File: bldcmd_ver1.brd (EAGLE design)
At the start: 43 x 49 mm, 90 parts, among them CN1 DF61-2P-2.2V(23), CN2 DF65-3P-1.7V(21), CN3 SM05B-SRSS-TB, CN4 SM04B-SRSS-TB, CN6 SM05B-SRSS-TB, CN7 SM04B-SRSS-TB, IC1 STSPIN32F0A, IC2 AS5047P-ATSM, IC3 ADM4852ACPZ-REEL7, Q1 PSMN2R4-30MLD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

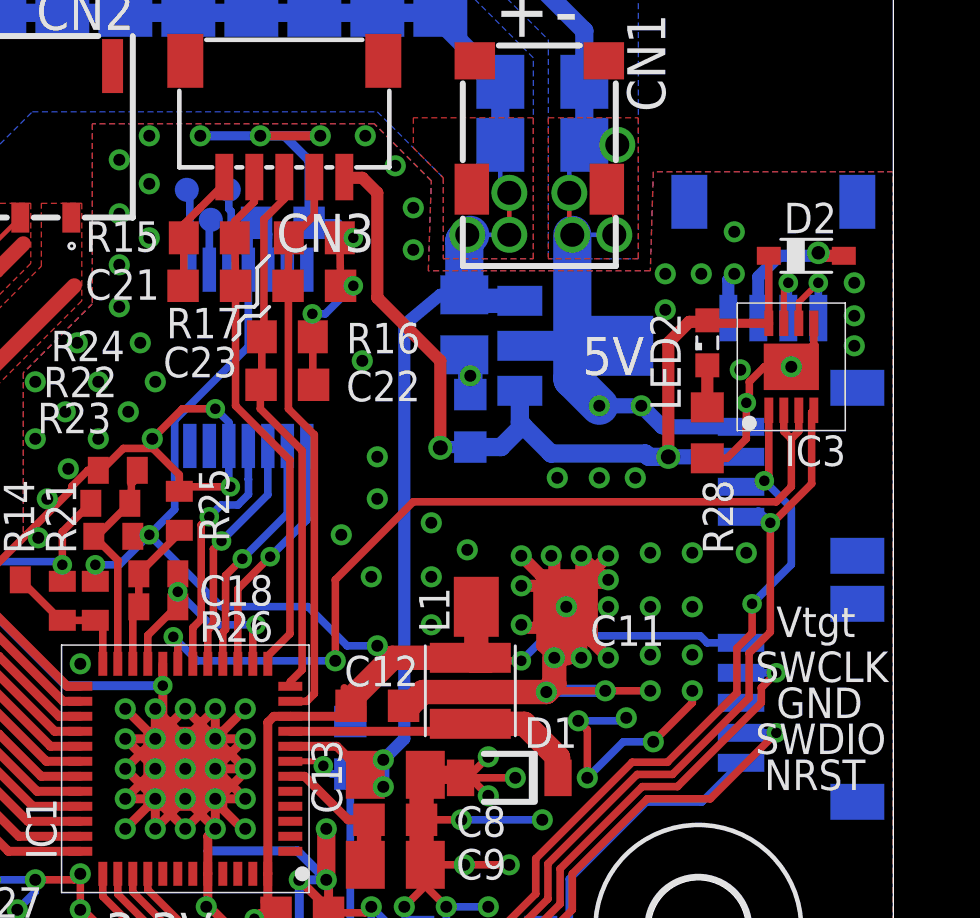
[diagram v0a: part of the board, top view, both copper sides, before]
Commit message: 部品に必要な値を割り当てた，（最適なのか？） BOM出した
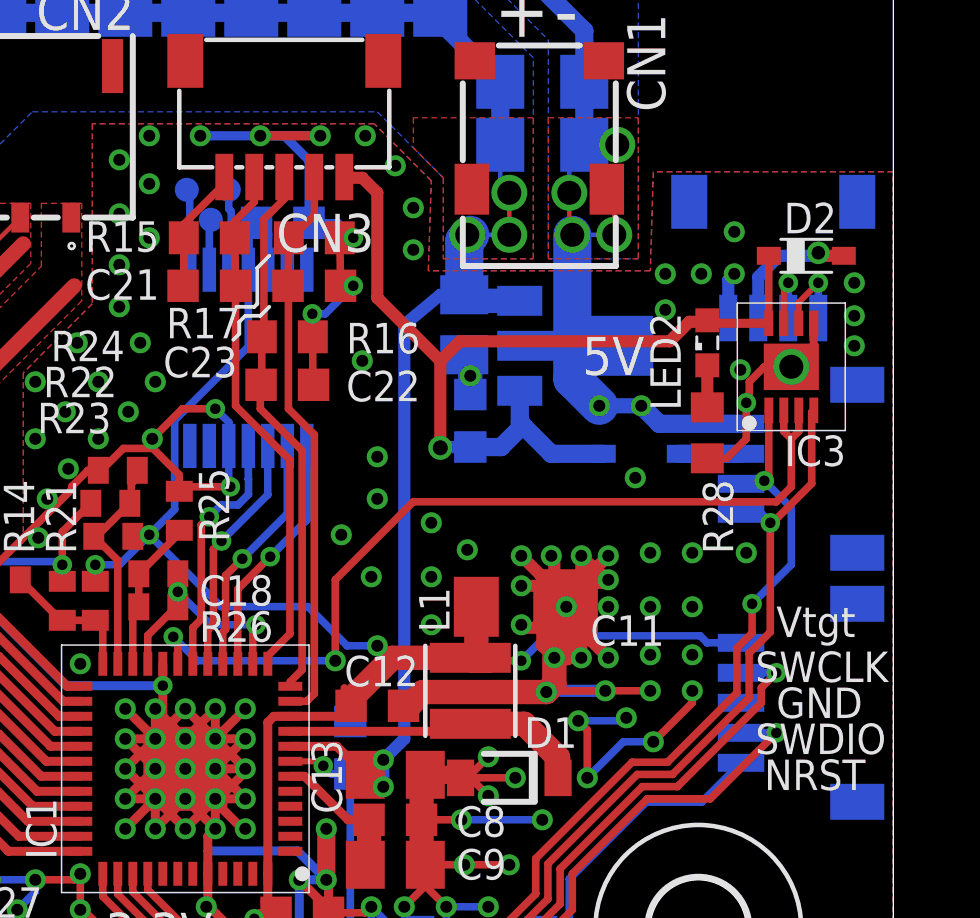
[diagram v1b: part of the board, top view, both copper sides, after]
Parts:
- removed CN4: SM04B-SRSS-TB, scramble-con-jst:SM04B-SRSS-TB
- added CN5: SM04B-SRSS-TB, scramble-con-jst:SM04B-SRSS-TB
- added D3: BAT60J, diode:SOD323_ST
- C1, C2, C3: value (none) -> 0.1u
- C17, C18: value (none) -> 100p
- L1: device rcssl_lib:SRN3015 -> scramble-mcu:SRN3015
- R1, R2, R3, R4, R5, R6: value (none) -> 20
- R10, R11, R12, R29, R7, R8, R9: value (none) -> 10k
- R14, R26: value (none) -> 15k
- R21: value (none) -> NP
- R22, R24: value (none) -> 560
- R23: value (none) -> 8.2k
- R25, R27, R28: value (none) -> 1k
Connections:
- new net N$10: CN5.2, D3.A
- net +5V: now also D3.C; no longer CN4.2
- net GND: now also CN5.1; no longer CN4.1
- net UART_RX: now also CN5.3; no longer CN4.3
- net UART_TX: now also CN5.4; no longer CN4.4
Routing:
- net N$10: track 0.00 -> 2.07 mm
- net +5V: track 32.4 -> 31.8 mm, vias 2 -> 1
- net GND: vias 149 -> 147

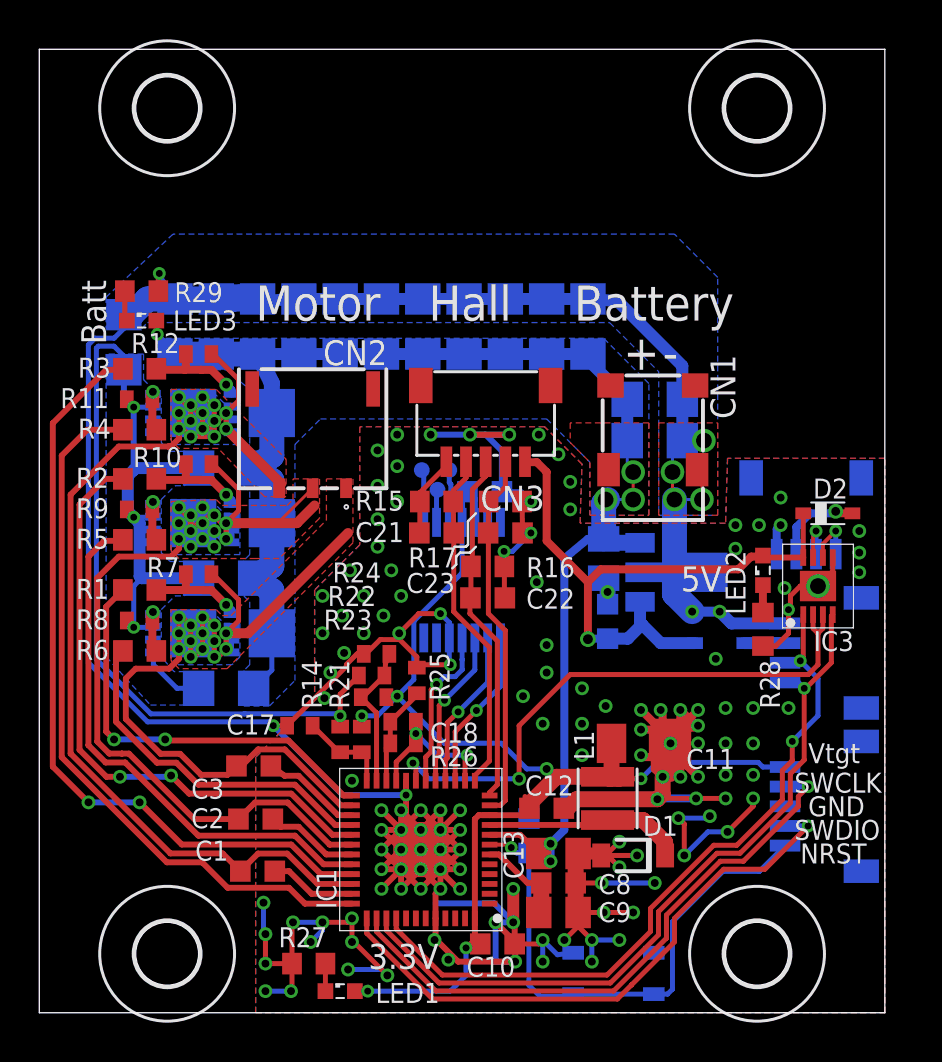
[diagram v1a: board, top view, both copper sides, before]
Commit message: AWを修正，コネクタの変更を適用
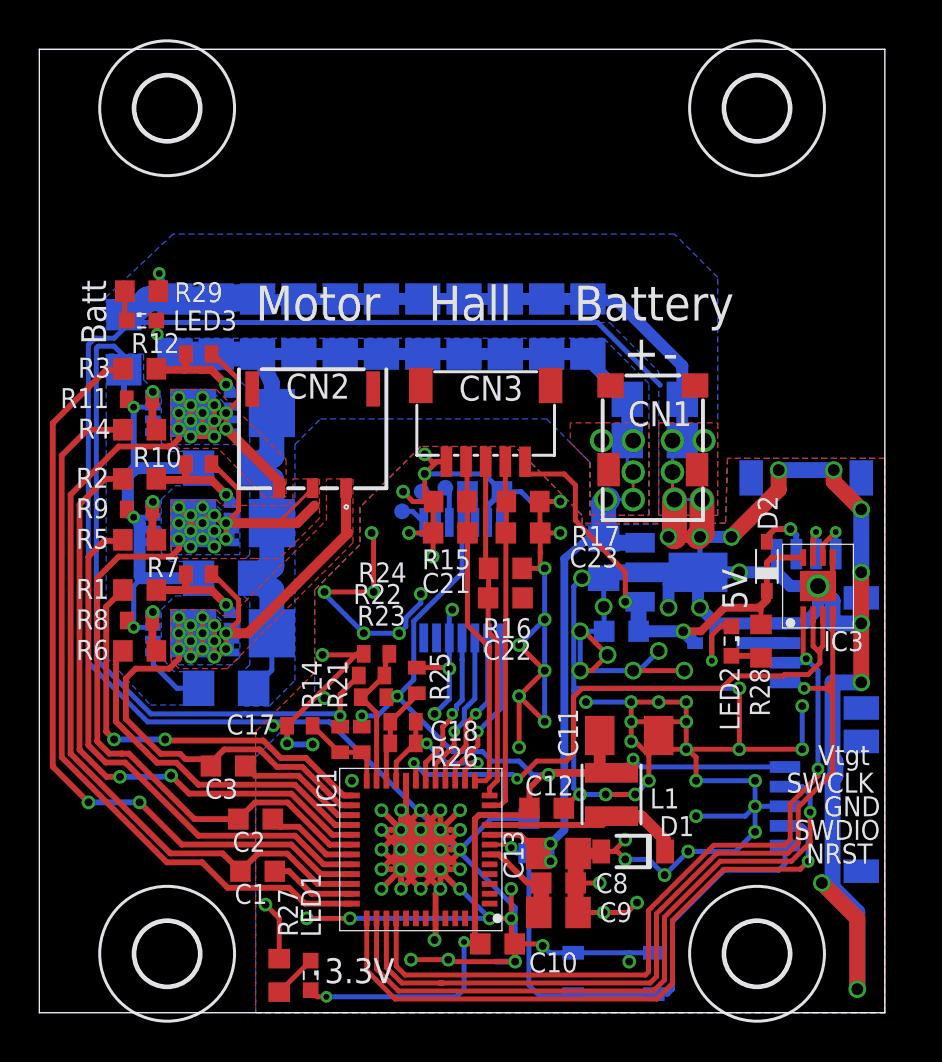
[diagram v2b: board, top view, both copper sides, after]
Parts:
- moved D2 4.11 mm to (37.0, 22.7), turned to 90 degrees
- moved LED2 3.94 mm to (35.2, 18.9), turned to 270 degrees
- moved TP3 2.33 mm to (18.4, 25.5)
- moved LED1 1.70 mm to (13.8, 1.90), turned to 270 degrees
- moved R27 1.62 mm to (12.2, 1.90), turned to 270 degrees
- moved C3 1.30 mm to (9.60, 12.6)
- moved TP1 0.92 mm to (20.6, 26.7)
- moved R16 0.91 mm to (23.7, 22.6)
- moved C23 0.90 mm to (24.6, 24.4)
- moved R17 0.90 mm to (24.6, 26.0)
- moved C22 0.90 mm to (23.7, 21.1)
- moved C19 0.86 mm to (29.6, 19.4), turned to 0 degrees
- moved TP2 0.81 mm to (19.4, 26.5)
- moved C11 0.72 mm to (30.0, 14.1)
- moved C21 0.70 mm to (20.9, 24.4)
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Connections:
- removed net N$33: LED2.C, R28.2
- new net N$21: LED2.A, R28.1
- net +5V: now also R28.2; no longer LED2.A
- net GND: now also LED2.C; no longer R28.1
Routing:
- net GND: track 300.1 -> 472.8 mm, vias 147 -> 124
- net +5V: track 31.8 -> 25.9 mm, vias 1 -> 2
- net UART_TX: track 39.2 -> 44.3 mm
- net SWCLK: track 30.3 -> 34.0 mm
- net UART_RX: track 37.2 -> 40.8 mm
- net SWDIO: track 30.1 -> 33.3 mm
- net +3V3: track 62.3 -> 65.3 mm
- net MOT_W: track 44.3 -> 46.4 mm
- net N$30: track 4.60 -> 3.01 mm
- net N$21: track 0.00 -> 1.54 mm
- net N$33: track 1.40 -> 0.00 mm
- net N$6: track 2.70 -> 1.33 mm
- net N$1: track 5.11 -> 6.46 mm
- net RTS: track 29.6 -> 30.7 mm
- net N$2: track 2.73 -> 1.84 mm
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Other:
- board text added: "RESET"
- board text added: "Scramble BLDC_MotorDriver v1.0"

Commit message: シルクの修正 これで発注した
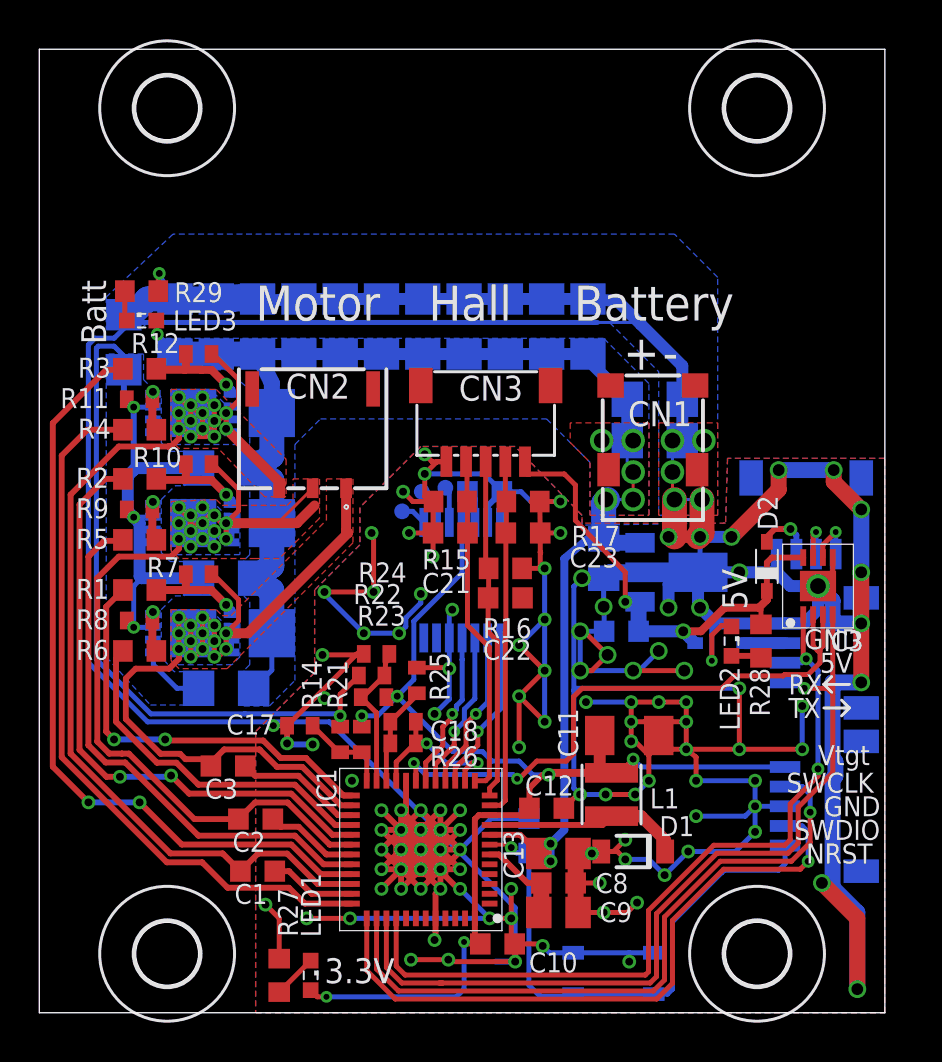
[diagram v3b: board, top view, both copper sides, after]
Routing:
- net GND: track 472.8 -> 470.7 mm, vias 124 -> 125
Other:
- board text added: "RX"
- board text added: "TX"
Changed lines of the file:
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@@
 <setting verticaltext="up"/>
 </settings>
-<grid distance="0.2" unitdist="mm" unit="mm" style="lines" multiple="1" display="yes" altdistance="0.05" altunitdist="mm" altunit="mm"/>
+<grid distance="0.1" unitdist="mm" unit="mm" style="lines" multiple="1" display="yes" altdistance="0.05" altunitdist="mm" altunit="mm"/>
 <layers>
 <layer number="1" name="Top" color="4" fill="1" visible="yes" active="yes"/>
@@
 <text x="14.5" y="1.5" size="1.27" layer="21" ratio="12">3.3V</text>
 <text x="36" y="20.5" size="1.27" layer="21" ratio="12" rot="R90">5V</text>
-<text x="3.4" y="34" size="1.27" layer="21" rot="R90">Batt</text>
+<text x="3.4" y="34" size="1.27" layer="21" ratio="12" rot="R90">Batt</text>
 <text x="39.9" y="10.5" size="1.016" layer="21" ratio="12" align="center-left">GND</text>
 <text x="38" y="11.7" size="1.016" layer="21" ratio="12" align="center-left">SWCLK</text>
@@
 BLDC_MotorDriver
 v1.0</text>
+<text x="38.1" y="16.7" size="1.016" layer="21" ratio="12" align="center-left">RX</text>
+<text x="38.1" y="15.5" size="1.016" layer="21" ratio="12" align="center-left">TX</text>
+<text x="39.7" y="17.8" size="1.016" layer="21" ratio="12" align="center-left">5V</text>
+<text x="38.9" y="19" size="1.016" layer="21" ratio="12" align="center-left">GND</text>
+<wire x1="39.9" y1="16.7" x2="41.2" y2="16.7" width="0.1524" layer="21"/>
+<wire x1="39.9" y1="15.5" x2="41.2" y2="15.5" width="0.1524" layer="21"/>
+<wire x1="39.9" y1="16.7" x2="40.3" y2="17.1" width="0.1524" layer="21"/>
+<wire x1="39.9" y1="16.7" x2="40.3" y2="16.3" width="0.1524" layer="21"/>
+<wire x1="41.2" y1="15.5" x2="40.8" y2="15.9" width="0.1524" layer="21"/>
+<wire x1="41.2" y1="15.5" x2="40.8" y2="15.1" width="0.1524" layer="21"/>
 </plain>
 <attributes>
@@
 </element>
 <element name="U$6" library="scramble-mcu" package="SOT89R" value="NJM78L05S" x="32.3" y="22.4" smashed="yes" rot="MR90">
-<attribute name="NAME" x="32.095" y="19.645" size="1.016" layer="26" rot="MR180"/>
+<attribute name="NAME" x="34.295" y="21.045" size="1.016" layer="26" rot="MR180"/>
 <attribute name="VALUE" x="28.475" y="20.195" size="1.27" layer="28" rot="MR90"/>
 </element>
@@
 <vertex x="16.3" y="23.8"/>
 <vertex x="14" y="21.5"/>
-<vertex x="14" y="16"/>
-<vertex x="11" y="13"/>
+<vertex x="14" y="17.3"/>
+<vertex x="11" y="14.3"/>
 <vertex x="11" y="0"/>
 </polygon>
@@
 <wire x1="32.7" y1="29.1" x2="32.7" y2="31.2" width="0.6096" layer="16"/>
 <wire x1="32.7" y1="31.2" x2="32.7" y2="32.9" width="0.6096" layer="16"/>
-<wire x1="32.7" y1="32.9" x2="29.4" y2="36.2" width="0.6096" layer="16"/>
+<wire x1="30.6" y1="35" x2="32.7" y2="32.9" width="0.6096" layer="16"/>
+<wire x1="30.6" y1="35" x2="29.4" y2="36.2" width="0.6096" layer="16"/>
 <wire x1="29.4" y1="36.2" x2="27.9" y2="36.3" width="0.6096" layer="16"/>
 <wire x1="27.9" y1="36.3" x2="25.8" y2="36.3" width="0.6096" layer="16"/>
@@
 <contactref element="CN5" pad="1"/>
 <contactref element="LED2" pad="C"/>
-<wire x1="27.4" y1="8.1" x2="28.475" y2="8.1" width="0.6096" layer="1"/>
+<wire x1="27.4" y1="8.1" x2="28.1" y2="8.1" width="0.6096" layer="1"/>
+<wire x1="28.1" y1="8.1" x2="28.475" y2="8.1" width="0.6096" layer="1"/>
 <wire x1="28.475" y1="8.1" x2="28.575" y2="8.2" width="0.6096" layer="1"/>
 <wire x1="24.2" y1="2.6" x2="20.9" y2="2.6" width="0.254" layer="1"/>
@@
 <wire x1="2.4936" y1="33.9683375" x2="2.8316625" y2="34.3064" width="0.254" layer="16"/>
 <wire x1="14.74825" y1="14.7936" x2="11.7064" y2="14.7936" width="0.254" layer="16"/>
-<wire x1="4.3" y1="35.1068" x2="28.38833125" y2="35.1068" width="0.254" layer="16"/>
-<wire x1="28.38833125" y1="35.1068" x2="31.5794" y2="31.91573125" width="0.254" layer="16"/>
+<wire x1="4.3" y1="35.1068" x2="28.2" y2="35.1068" width="0.254" layer="16"/>
+<wire x1="28.2" y1="35.1068" x2="28.38833125" y2="35.1068" width="0.254" layer="16"/>
 <wire x1="24.2" y1="2.6" x2="24.2" y2="5.34185" width="0.254" layer="16"/>
 <wire x1="24.2" y1="5.34185" x2="14.74825" y2="14.7936" width="0.254" layer="16"/>
@@
 <via x="16.9" y="24.4" extent="1-16" drill="0.4"/>
 <via x="32.2" y="29.1" extent="1-16" drill="0.8"/>
+<wire x1="28.2" y1="35.1068" x2="30.4932" y2="35.1068" width="0.1524" layer="16"/>
+<wire x1="30.4932" y1="35.1068" x2="30.6" y2="35" width="0.1524" layer="16"/>
+<via x="28.1" y="8.1" extent="1-16" drill="0.4"/>
 </signal>
 <signal name="+3V3">

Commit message: BSコンデンサを0402inchに変更 デバッグ用のLEDを追加 BOOT0のプルダウン抵抗の追加( #4)
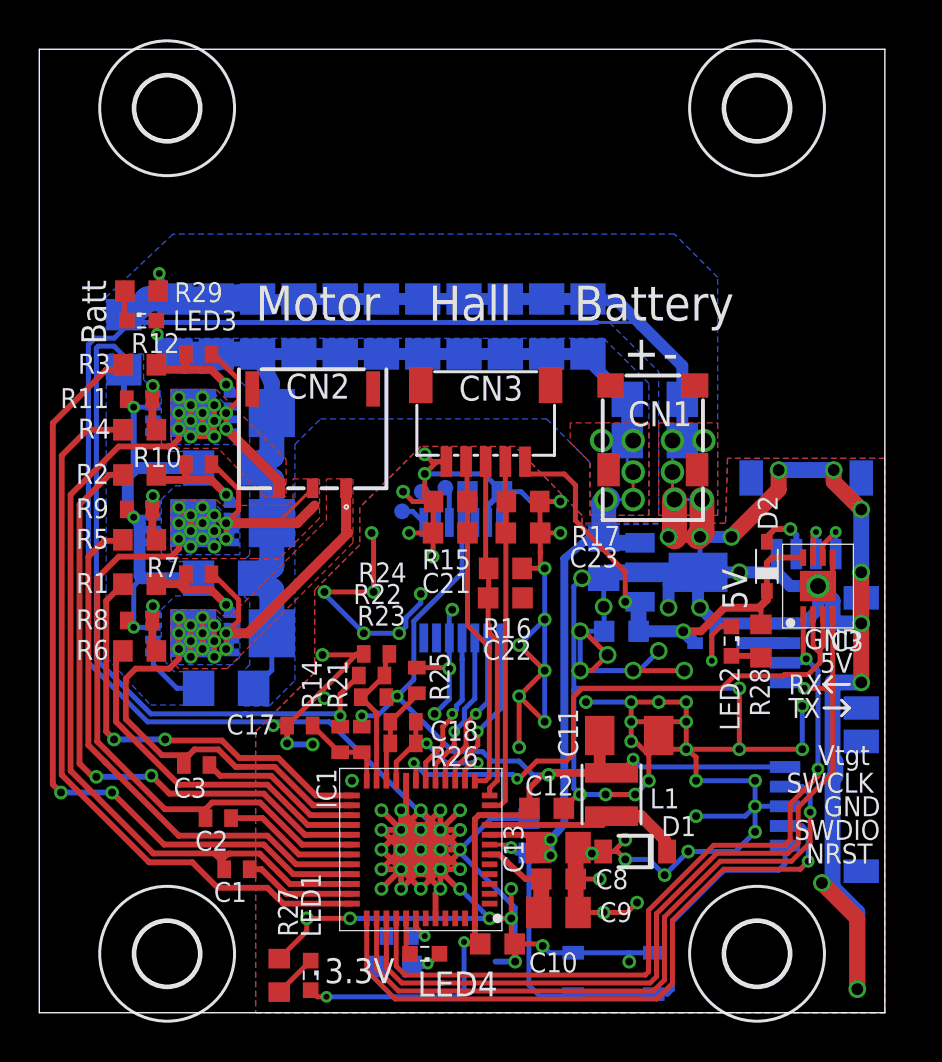
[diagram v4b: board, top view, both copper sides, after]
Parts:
- added LED4: (no value), led:SML0603
- added R18: 10k, rcl:R0402
- added R19: 1k, rcl:R0603
- C1, C2, C3: device rcl:C0603K -> rcl:C0402
- moved C2 1.90 mm to (9.10, 9.90)
- moved C3 1.60 mm to (8.00, 12.6)
- moved C1 1.05 mm to (10.1, 7.30)
- moved C13 0.30 mm to (26.4, 8.40)
- moved R1 0.30 mm to (5.10, 21.8)
- moved R2 0.20 mm to (5.10, 27.4)
- moved R3 0.20 mm to (5.10, 33.0)
- moved C8 0.20 mm to (26.4, 6.80)
- moved D1 0.10 mm to (30.3, 8.20)
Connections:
- new net N$22: IC1.42, R18.1
- new net N$33: LED4.C, R19.2
- new net N$37: IC1.41, LED4.A
- net GND: now also R18.2, R19.1
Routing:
- net GND: track 470.7 -> 466.5 mm, vias 125 -> 121
- net N$4: track 4.77 -> 6.92 mm
- net N$37: track 0.00 -> 1.88 mm
- net N$1: track 6.46 -> 8.31 mm
- net N$22: track 0.00 -> 1.74 mm, vias 0 -> 1
- net N$33: track 0.00 -> 1.67 mm, vias 0 -> 1
- net N$5: track 4.40 -> 5.72 mm
- net MOT_U: track 56.8 -> 58.0 mm
- net N$15: track 2.52 -> 3.42 mm
- net HS_U: track 39.7 -> 40.4 mm
- net N$14: track 2.13 -> 2.73 mm
- net N$16: track 2.17 -> 2.77 mm
- net LS_U: track 36.8 -> 37.4 mm
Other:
- board text added: "Scramble BLDC_MotorDriver v1.1"
- board text removed: "Scramble BLDC_MotorDriver v1.0"

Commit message: REG12のコンデンサの位置を調整
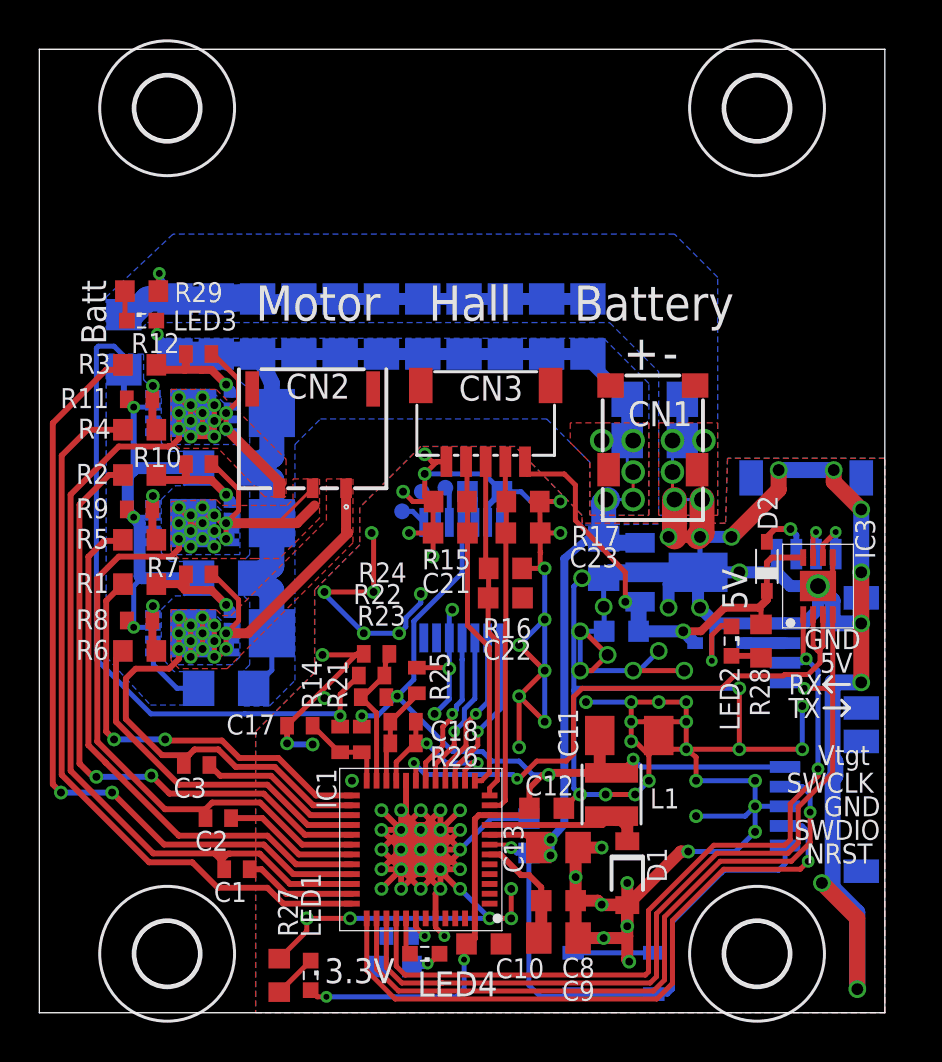
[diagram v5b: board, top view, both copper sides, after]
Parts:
- moved C9 1.30 mm to (26.4, 3.80)
- moved D1 1.17 mm to (29.9, 7.10), turned to 270 degrees
- moved C8 1.10 mm to (26.4, 5.70)
- moved C10 0.70 mm to (22.6, 3.50)
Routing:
- net GND: track 466.5 -> 382.9 mm, vias 121 -> 118
- net N$18: track 10.2 -> 8.17 mm
- net N$19: track 4.87 -> 5.95 mm
- net +3V3: track 65.3 -> 64.6 mm
